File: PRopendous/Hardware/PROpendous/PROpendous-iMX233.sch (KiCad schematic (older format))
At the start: 19 parts, among them IC1 i.MX233, SW1 POWER, X1 24MHz

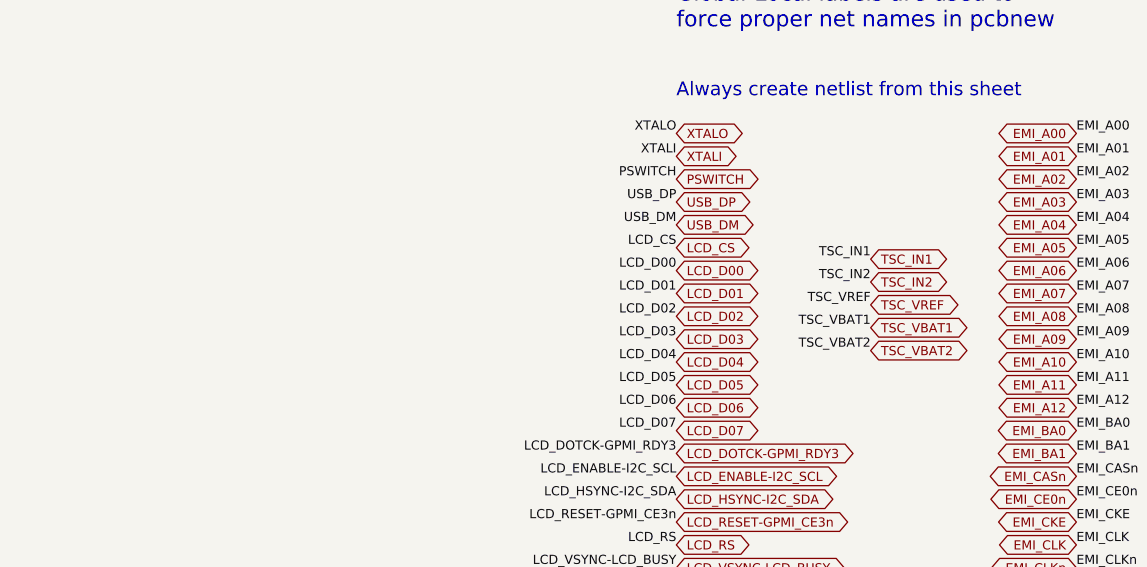
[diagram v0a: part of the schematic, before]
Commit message: Updated i.MX233-based PROpendous board with EEPROM to fix Freescale Errata #2229.
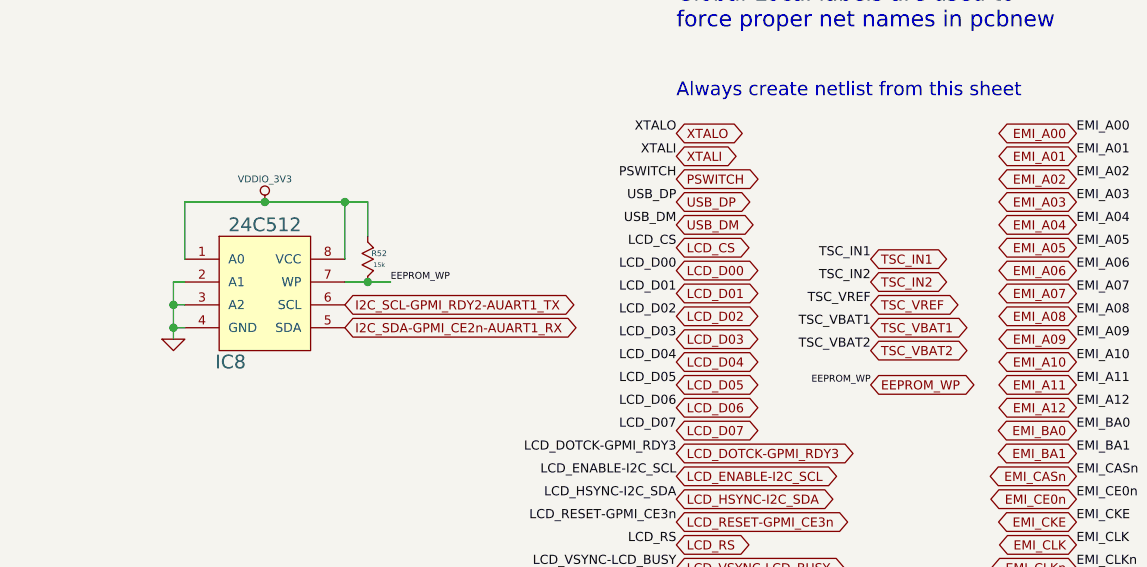
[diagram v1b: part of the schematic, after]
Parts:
- added IC8: 24C512, symbol 24C512
- added R52: 15k, symbol R_MINI
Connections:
- net labels added: EEPROM_WP
- wire segments 52 -> 61
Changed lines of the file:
@@
-EESchema Schematic File Version 2  date 26/04/2010 13:13:01
+EESchema Schematic File Version 2  date 27/04/2010 18:25:33
 LIBS:opendous
 LIBS:device
@@
 Sheet 2 8
 Title "PROpendous"
-Date "26 apr 2010"
+Date "27 apr 2010"
 Rev "1.0"
 Comp "Opendous Inc. (www.opendous.org)"
@@
 Comment4 "www.PROpendous.org"
 $EndDescr
+Text GLabel 9900 2450 2    40   BiDi ~ 0
+EEPROM_WP
+Connection ~ 7700 2000
+Wire Wire Line
+	7800 2000 7600 2000
+Connection ~ 6850 2200
+Wire Wire Line
+	6850 2100 6900 2100
+Connection ~ 7250 1650
+Wire Wire Line
+	6900 1900 6900 1650
 Connection ~ 7450 6050
 Connection ~ 7250 6050
@@
 	7250 6050 7250 5850
 Connection ~ 7450 5950
+Wire Wire Line
+	7600 1650 7600 1900
+Wire Wire Line
+	6850 2200 6900 2200
+Wire Wire Line
+	6900 2000 6850 2000
+Wire Wire Line
+	6850 2000 6850 2250
+Connection ~ 6850 2100
+Wire Wire Line
+	7700 1800 7700 1650
+Wire Wire Line
+	7700 1650 6900 1650
+Connection ~ 7600 1650
+Text Label 9900 2450 2    30   ~ 0
+EEPROM_WP
+Text Label 7800 2000 0    30   ~ 0
+EEPROM_WP
+Text GLabel 7600 2200 2    40   BiDi ~ 0
+I2C_SDA-GPMI_CE2n-AUART1_RX
+Text GLabel 7600 2100 2    40   BiDi ~ 0
+I2C_SCL-GPMI_RDY2-AUART1_TX
+$Comp
+L R_MINI R52
+U 1 1 4BD75B1B
+P 7700 1900
+F 0 "R52" V 7675 1950 25  0000 C CNN
+F 1 "15k" V 7725 1950 20  0000 C CNN
+	1    7700 1900
+	0    1    1    0
+$EndComp
+$Comp
+L GND #PWR01
+U 1 1 4BD75A47
+P 6850 2250
+F 0 "#PWR01" H 6850 2250 30  0001 C CNN
+F 1 "GND" H 6850 2180 30  0001 C CNN
+	1    6850 2250
+	1    0    0    -1
+$EndComp
+$Comp
+L VDDIO_3V3 #PWR02
+U 1 1 4BD75A3A
+P 7250 1650
+F 0 "#PWR02" H 7250 1750 30  0001 C CNN
+F 1 "VDDIO_3V3" H 7250 1750 30  0000 C CNN
+	1    7250 1650
+	1    0    0    -1
+$EndComp
+$Comp
+L 24C512 IC8
+U 1 1 4BD75A33
+P 7250 2050
+F 0 "IC8" H 7100 1750 60  0000 C CNN
+F 1 "24C512" H 7250 2350 60  0000 C CNN
+	1    7250 2050
+	1    0    0    -1
+$EndComp
 $Comp
 L IMX233 IC1
@@
 $EndComp
 $Comp
-L GND #PWR01
+L GND #PWR03
 U 1 1 4BCCECE8
 P 6450 7500
-F 0 "#PWR01" H 6450 7500 30  0001 C CNN
+F 0 "#PWR03" H 6450 7500 30  0001 C CNN
 F 1 "GND" H 6450 7430 30  0001 C CNN
 	1    6450 7500
@@
 $EndComp
 $Comp
-L GND1 #PWR02
+L GND1 #PWR04
 U 1 1 4BCCECDD
 P 6150 7500
-F 0 "#PWR02" H 6150 7500 30  0001 C CNN
+F 0 "#PWR04" H 6150 7500 30  0001 C CNN
 F 1 "GND1" H 6150 7430 30  0000 C CNN
 	1    6150 7500
@@
 Use GNDPWR for chassis\nground ring to suppress EMI
 $Comp
-L GND #PWR03
+L GND #PWR05
 U 1 1 4BCC48BC
 P 7500 6100
-F 0 "#PWR03" H 7500 6100 30  0001 C CNN
+F 0 "#PWR05" H 7500 6100 30  0001 C CNN
 F 1 "GND" H 7500 6030 30  0001 C CNN
 	1    7500 6100
@@
 $EndComp
 $Comp
-L GNDPWR #PWR04
+L GNDPWR #PWR06
 U 1 1 4BCC48B6
 P 7200 6100
-F 0 "#PWR04" H 7200 6150 40  0001 C CNN
+F 0 "#PWR06" H 7200 6150 40  0001 C CNN
 F 1 "GNDPWR" H 7200 6040 25  0000 C CNN
 	1    7200 6100
@@
 $EndComp
 $Comp
-L VDDIO_3V3 #PWR05
+L VDDIO_3V3 #PWR07
 U 1 1 4BC3A9DE
 P 5100 700
-F 0 "#PWR05" H 5100 800 30  0001 C CNN
+F 0 "#PWR07" H 5100 800 30  0001 C CNN
 F 1 "VDDIO_3V3" H 5100 800 30  0000 C CNN
 	1    5100 700
@@
 $EndComp
 $Comp
-L GNDPWR #PWR06
+L GNDPWR #PWR08
 U 1 1 4BBD1ABB
 P 7350 5300
-F 0 "#PWR06" H 7350 5350 40  0001 C CNN
+F 0 "#PWR08" H 7350 5350 40  0001 C CNN
 F 1 "GNDPWR" H 7350 5240 25  0000 C CNN
 	1    7350 5300
@@
 $EndComp
 $Comp
-L HP_VGND #PWR07
+L HP_VGND #PWR09
 U 1 1 4BBCE7B9
 P 4550 7350
-F 0 "#PWR07" H 4550 7350 30  0001 C CNN
+F 0 "#PWR09" H 4550 7350 30  0001 C CNN
 F 1 "HP_VGND" H 4550 7280 30  0000 C CNN
 	1    4550 7350
@@
 PSWITCH
 $Comp
-L GND #PWR08
+L GND #PWR010
 U 1 1 4BBCDC88
 P 1200 2100
-F 0 "#PWR08" H 1200 2100 30  0001 C CNN
+F 0 "#PWR010" H 1200 2100 30  0001 C CNN
 F 1 "GND" H 1200 2030 30  0001 C CNN
 	1    1200 2100
@@
 $EndComp
 $Comp
-L VDD_XTAL #PWR09
+L VDD_XTAL #PWR011
 U 1 1 4BBCDC06
 P 650 1350
-F 0 "#PWR09" H 650 1450 30  0001 C CNN
+F 0 "#PWR011" H 650 1450 30  0001 C CNN
 F 1 "VDD_XTAL" H 650 1450 30  0000 C CNN
 	1    650  1350
@@
 $EndComp
 $Comp
-L GND #PWR010
+L GND #PWR012
 U 1 1 4BBCDB43
 P 650 2100
-F 0 "#PWR010" H 650 2100 30  0001 C CNN
+F 0 "#PWR012" H 650 2100 30  0001 C CNN
 F 1 "GND" H 650 2030 30  0001 C CNN
 	1    650  2100
@@
 $EndComp
 $Comp
-L VDD_XTAL #PWR011
+L VDD_XTAL #PWR013
 U 1 1 4BBCDB1B
 P 650 1800
-F 0 "#PWR011" H 650 1900 30  0001 C CNN
+F 0 "#PWR013" H 650 1900 30  0001 C CNN
 F 1 "VDD_XTAL" H 650 1900 30  0000 C CNN
 	1    650  1800
@@
 $EndComp
 $Comp
-L VDD5V #PWR012
+L VDD5V #PWR014
 U 1 1 4BBCD826
 P 4300 700
-F 0 "#PWR012" H 4300 800 30  0001 C CNN
+F 0 "#PWR014" H 4300 800 30  0001 C CNN
 F 1 "VDD5V" H 4300 800 30  0000 C CNN
 	1    4300 700
@@
 $EndComp
 $Comp
-L GND #PWR013
+L GND #PWR015
 U 1 1 4BBCD031
 P 3950 7350
-F 0 "#PWR013" H 3950 7350 30  0001 C CNN
+F 0 "#PWR015" H 3950 7350 30  0001 C CNN
 F 1 "GND" H 3950 7280 30  0001 C CNN
 	1    3950 7350
@@
 $EndComp
 $Comp
-L GND #PWR014
+L GND #PWR016
 U 1 1 4BBCCF65
 P 1600 600
-F 0 "#PWR014" H 1600 600 30  0001 C CNN
+F 0 "#PWR016" H 1600 600 30  0001 C CNN
 F 1 "GND" H 1600 530 30  0001 C CNN
 	1    1600 600
@@
 GND1 must route to\nstar ground at VSSA2
 $Comp
-L GND1 #PWR015
+L GND1 #PWR017
 U 1 1 4BBCCEB7
 P 5850 7100
-F 0 "#PWR015" H 5850 7100 30  0001 C CNN
+F 0 "#PWR017" H 5850 7100 30  0001 C CNN
 F 1 "GND1" H 5850 7030 30  0000 C CNN
 	1    5850 7100
@@
 $EndComp
 $Comp
-L VDDM_2V5 #PWR016
+L VDDM_2V5 #PWR018
 U 1 1 4BBCCC9E
 P 4750 700
-F 0 "#PWR016" H 4750 800 30  0001 C CNN
+F 0 "#PWR018" H 4750 800 30  0001 C CNN
 F 1 "VDDM_2V5" H 4750 800 30  0000 C CNN
 	1    4750 700
@@
 $EndComp
 $Comp
-L VDD_XTAL #PWR017
+L VDD_XTAL #PWR019
 U 1 1 4BBCCC78
 P 4450 850
-F 0 "#PWR017" H 4450 950 30  0001 C CNN
+F 0 "#PWR019" H 4450 950 30  0001 C CNN
 F 1 "VDD_XTAL" H 4450 950 30  0000 C CNN
 	1    4450 850
@@
 $EndComp
 $Comp
-L VDDA #PWR018
+L VDDA #PWR020
 U 1 1 4BBCCB4A
 P 4100 700
-F 0 "#PWR018" H 4100 800 30  0001 C CNN
+F 0 "#PWR020" H 4100 800 30  0001 C CNN
 F 1 "VDDA" H 4100 800 30  0000 C CNN
 	1    4100 700
@@
 $EndComp
 $Comp
-L VDDD #PWR019
+L VDDD #PWR021
 U 1 1 4BBCCB16
 P 3800 700
-F 0 "#PWR019" H 3800 800 30  0001 C CNN
+F 0 "#PWR021" H 3800 800 30  0001 C CNN
 F 1 "VDDD" H 3800 800 30  0000 C CNN
 	1    3800 700
@@
 $EndComp
 $Comp
-L VDDIO_3V3 #PWR020
+L VDDIO_3V3 #PWR022
 U 1 1 4BBCC974
 P 3550 700
-F 0 "#PWR020" H 3550 800 30  0001 C CNN
+F 0 "#PWR022" H 3550 800 30  0001 C CNN
 F 1 "VDDIO_3V3" H 3550 800 30  0000 C CNN
 	1    3550 700
@@
 $EndComp
 $Comp
-L VDD4P2 #PWR021
+L VDD4P2 #PWR023
 U 1 1 4BBCC950
 P 3050 700
-F 0 "#PWR021" H 3050 800 30  0001 C CNN
+F 0 "#PWR023" H 3050 800 30  0001 C CNN
 F 1 "VDD4P2" H 3050 800 30  0000 C CNN
 	1    3050 700
@@
 $EndComp
 $Comp
-L VDD_BATT #PWR022
+L VDD_BATT #PWR024
 U 1 1 4BBCC942
 P 2800 700
-F 0 "#PWR022" H 2800 800 30  0001 C CNN
+F 0 "#PWR024" H 2800 800 30  0001 C CNN
 F 1 "VDD_BATT" H 2800 800 30  0000 C CNN
 	1    2800 700

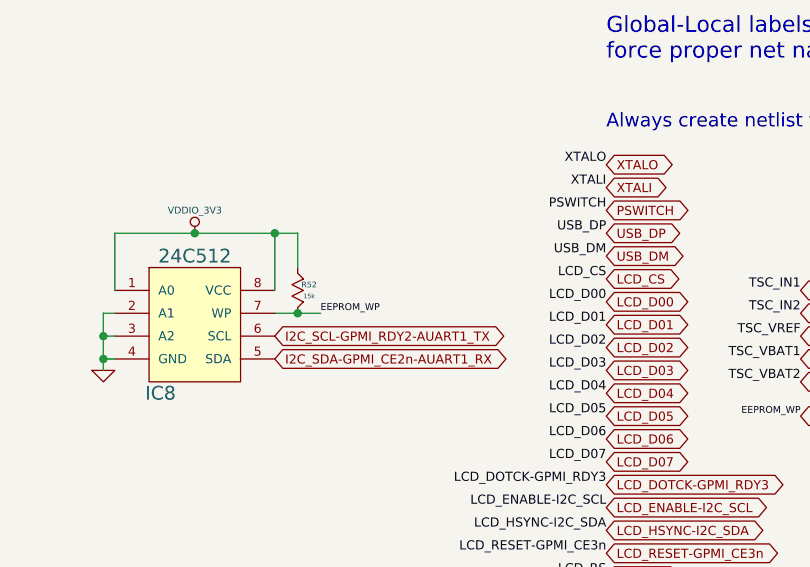
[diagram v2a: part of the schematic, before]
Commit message: Updated PROpendous design and manufacturing files.
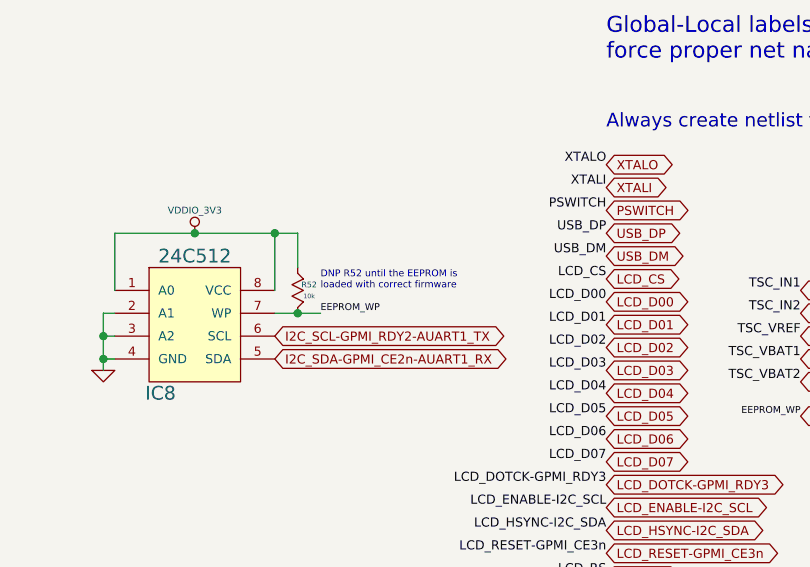
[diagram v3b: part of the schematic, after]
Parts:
- R52: value 15k -> 10k
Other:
- note added: "DNP R52 until the EEPROM is\nloaded with correct firmware"
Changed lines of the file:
@@
-EESchema Schematic File Version 2  date 07/05/2010 11:28:22
+EESchema Schematic File Version 2  date 18/05/2010 10:44:52
 LIBS:opendous
 LIBS:device
@@
 LIBS:valves
 LIBS:power
+LIBS:PROpendous-cache
 EELAYER 24  0
 EELAYER END
@@
 Sheet 2 8
 Title "PROpendous"
-Date "7 may 2010"
+Date "18 may 2010"
 Rev "1.0"
 Comp "Opendous Inc. (www.opendous.org)"
@@
 Comment4 "www.PROpendous.org"
 $EndDescr
+Text Notes 7800 1900 0    30   ~ 0
+DNP R52 until the EEPROM is\nloaded with correct firmware
 Text GLabel 9900 2450 2    40   BiDi ~ 0
 EEPROM_WP
@@
 P 7700 1900
 F 0 "R52" V 7675 1950 25  0000 C CNN
-F 1 "15k" V 7725 1950 20  0000 C CNN
+F 1 "10k" V 7725 1950 20  0000 C CNN
 	1    7700 1900
 	0    1    1    0

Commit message: Updated PROpendous with correct I2C EEPROM address.  Added pictures of the LPC3130 based PROpendous-DIY.
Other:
- note added: "I2C EEPROM Address = 0b1010000R = 0xA0 = 160"
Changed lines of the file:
@@
-EESchema Schematic File Version 2  date 31/05/2010 00:35:42
+EESchema Schematic File Version 2  date 07/06/2010 07:15:05
 LIBS:opendous
 LIBS:device
@@
 LIBS:valves
 LIBS:power
+LIBS:PROpendous-cache
 EELAYER 24  0
 EELAYER END
@@
 Sheet 2 8
 Title "PROpendous"
-Date "29 may 2010"
+Date "7 jun 2010"
 Rev "1.0"
 Comp "Opendous Inc. (www.opendous.org)"
@@
 Comment4 "www.PROpendous.org"
 $EndDescr
+Text Notes 6800 2500 0    40   ~ 0
+I2C EEPROM Address = 0b1010000R = 0xA0 = 160
+Connection ~ 6850 2000
+Wire Wire Line
+	6850 2250 6850 1900
+Wire Wire Line
+	6850 1900 6900 1900
+Connection ~ 7600 1650
+Wire Wire Line
+	7250 1650 7700 1650
+Wire Wire Line
+	7700 1650 7700 1800
+Connection ~ 6850 2100
+Wire Wire Line
+	6850 2000 6900 2000
+Wire Wire Line
+	6850 2200 6900 2200
+Wire Wire Line
+	7600 1650 7600 1900
+Connection ~ 7450 5950
+Wire Wire Line
+	7250 5850 7250 6050
+Wire Wire Line
+	7500 6100 7500 6050
+Wire Wire Line
+	7500 6050 7450 6050
+Connection ~ 4750 950
+Wire Wire Line
+	4750 950  4750 700
+Connection ~ 4800 950
+Wire Wire Line
+	5050 950  5150 950
+Wire Wire Line
+	7350 5300 7350 5250
+Connection ~ 3950 7250
+Wire Wire Line
+	3950 7250 3950 7350
+Connection ~ 4000 7250
+Connection ~ 3800 7250
+Wire Wire Line
+	1100 1250 1100 1200
+Wire Wire Line
+	1100 1550 1100 1450
+Wire Wire Line
+	1050 1500 1350 1500
+Wire Wire Line
+	1550 1500 2200 1500
+Wire Wire Line
+	1100 1850 1100 1750
+Wire Wire Line
+	1200 2100 1200 2050
+Wire Wire Line
+	650  2100 650  2050
+Wire Wire Line
+	5850 6800 5850 6700
+Wire Wire Line
+	5850 6700 5700 6700
+Connection ~ 1300 900
+Wire Wire Line
+	2200 1300 1300 1300
+Wire Wire Line
+	1300 1300 1300 750
+Connection ~ 1600 550
+Wire Wire Line
+	1600 600  1600 550
+Wire Wire Line
+	4450 850  4450 950
+Wire Wire Line
+	3550 950  3550 700
+Wire Wire Line
+	3800 700  3800 950
+Wire Wire Line
+	4150 950  4050 950
+Wire Wire Line
+	3200 900  3200 950
+Connection ~ 2800 950
+Wire Wire Line
+	2900 950  2800 950
+Wire Wire Line
+	2800 950  2800 700
+Wire Wire Line
+	3050 950  3050 700
+Wire Wire Line
+	3400 900  3400 950
+Wire Wire Line
+	4100 700  4100 950
+Connection ~ 4100 950
+Wire Wire Line
+	3900 950  3700 950
+Connection ~ 3800 950
+Wire Wire Line
+	4300 700  4300 950
+Wire Wire Line
+	1900 550  1300 550
+Wire Wire Line
+	1900 750  1900 1200
+Wire Wire Line
+	1900 1200 2200 1200
+Connection ~ 1900 900
+Wire Wire Line
+	5850 7000 5850 7100
+Wire Wire Line
+	650  1850 650  1800
+Wire Wire Line
+	750  1500 650  1500
+Wire Wire Line
+	1300 1900 1300 2050
+Wire Wire Line
+	1300 2050 1100 2050
+Connection ~ 1200 2050
+Wire Wire Line
+	650  1500 650  1350
+Connection ~ 1100 1500
+Wire Wire Line
+	1300 1700 1300 1500
+Connection ~ 1300 1500
+Connection ~ 3900 7250
+Wire Wire Line
+	4250 7250 3650 7250
+Connection ~ 4150 7250
+Wire Wire Line
+	4550 7350 4550 7250
+Wire Wire Line
+	4600 950  4900 950
+Connection ~ 4700 950
+Wire Wire Line
+	5100 700  5100 950
+Connection ~ 5100 950
+Wire Wire Line
+	7250 6050 7200 6050
+Wire Wire Line
+	7200 6050 7200 6100
+Wire Wire Line
+	6150 7500 6150 7450
+Wire Wire Line
+	6150 7450 6200 7450
+Wire Wire Line
+	6400 7450 6450 7450
+Wire Wire Line
+	6450 7450 6450 7500
+Connection ~ 7250 5950
+Wire Wire Line
+	7450 6050 7450 5850
+Connection ~ 7250 6050
+Connection ~ 7450 6050
+Wire Wire Line
+	6850 2100 6900 2100
+Connection ~ 6850 2200
+Wire Wire Line
+	7600 2000 7800 2000
+Connection ~ 7700 2000
 Text Notes 7800 1900 0    30   ~ 0
 DNP R52 until the EEPROM is\nloaded with correct firmware
 Text GLabel 9900 2450 2    40   BiDi ~ 0
 EEPROM_WP
-Connection ~ 7700 2000
-Wire Wire Line
-	7800 2000 7600 2000
-Connection ~ 6850 2200
-Wire Wire Line
-	6850 2100 6900 2100
-Connection ~ 7250 1650
-Wire Wire Line
-	6900 1900 6900 1650
-Connection ~ 7450 6050
-Connection ~ 7250 6050
-Wire Wire Line
-	7450 5850 7450 6050
-Connection ~ 7250 5950
-Wire Wire Line
-	6450 7500 6450 7450
-Wire Wire Line
-	6450 7450 6400 7450
-Wire Wire Line
-	6200 7450 6150 7450
-Wire Wire Line
-	6150 7450 6150 7500
-Wire Wire Line
-	7200 6100 7200 6050
-Wire Wire Line
-	7200 6050 7250 6050
-Connection ~ 5100 950
-Wire Wire Line
-	5100 700  5100 950
-Connection ~ 4700 950
-Wire Wire Line
-	4900 950  4600 950
-Wire Wire Line
-	4550 7350 4550 7250
-Connection ~ 4150 7250
-Wire Wire Line
-	3650 7250 4250 7250
-Connection ~ 3900 7250
-Connection ~ 1300 1500
-Wire Wire Line
-	1300 1700 1300 1500
-Connection ~ 1100 1500
-Wire Wire Line
-	650  1350 650  1500
-Connection ~ 1200 2050
-Wire Wire Line
-	1100 2050 1300 2050
-Wire Wire Line
-	1300 2050 1300 1900
-Wire Wire Line
-	650  1500 750  1500
-Wire Wire Line
-	650  1850 650  1800
-Wire Wire Line
-	5850 7000 5850 7100
-Connection ~ 1900 900
-Wire Wire Line
-	2200 1200 1900 1200
-Wire Wire Line
-	1900 1200 1900 750
-Wire Wire Line
-	1300 550  1900 550
-Wire Wire Line
-	4300 700  4300 950
-Connection ~ 3800 950
-Wire Wire Line
-	3700 950  3900 950
-Connection ~ 4100 950
-Wire Wire Line
-	4100 700  4100 950
-Wire Wire Line
-	3400 900  3400 950
-Wire Wire Line
-	3050 950  3050 700
-Wire Wire Line
-	2800 700  2800 950
-Wire Wire Line
-	2800 950  2900 950
-Connection ~ 2800 950
-Wire Wire Line
-	3200 900  3200 950
-Wire Wire Line
-	4050 950  4150 950
-Wire Wire Line
-	3800 700  3800 950
-Wire Wire Line
-	3550 950  3550 700
-Wire Wire Line
-	4450 850  4450 950
-Wire Wire Line
-	1600 600  1600 550
-Connection ~ 1600 550
-Wire Wire Line
-	1300 750  1300 1300
-Wire Wire Line
-	1300 1300 2200 1300
-Connection ~ 1300 900
-Wire Wire Line
-	5700 6700 5850 6700
-Wire Wire Line
-	5850 6700 5850 6800
-Wire Wire Line
-	650  2100 650  2050
-Wire Wire Line
-	1200 2100 1200 2050
-Wire Wire Line
-	1100 1850 1100 1750
-Wire Wire Line
-	1550 1500 2200 1500
-Wire Wire Line
-	1350 1500 1050 1500
-Wire Wire Line
-	1100 1450 1100 1550
-Wire Wire Line
-	1100 1250 1100 1200
-Connection ~ 3800 7250
-Connection ~ 4000 7250
-Wire Wire Line
-	3950 7250 3950 7350
-Connection ~ 3950 7250
-Wire Wire Line
-	7350 5300 7350 5250
-Wire Wire Line
-	5150 950  5050 950
-Connection ~ 4800 950
-Wire Wire Line
-	4750 950  4750 700
-Connection ~ 4750 950
-Wire Wire Line
-	7450 6050 7500 6050
-Wire Wire Line
-	7500 6050 7500 6100
-Wire Wire Line
-	7250 6050 7250 5850
-Connection ~ 7450 5950
-Wire Wire Line
-	7600 1650 7600 1900
-Wire Wire Line
-	6850 2200 6900 2200
-Wire Wire Line
-	6900 2000 6850 2000
-Wire Wire Line
-	6850 2000 6850 2250
-Connection ~ 6850 2100
-Wire Wire Line
-	7700 1800 7700 1650
-Wire Wire Line
-	7700 1650 6900 1650
-Connection ~ 7600 1650
 Text Label 9900 2450 2    30   ~ 0
 EEPROM_WP

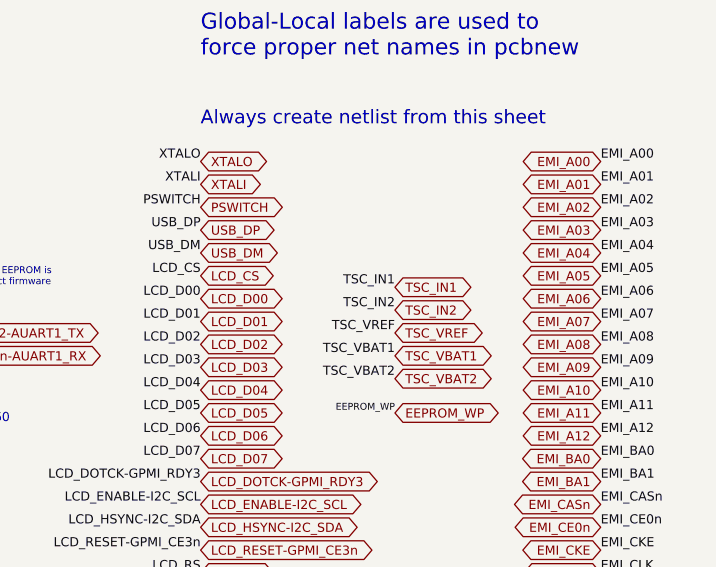
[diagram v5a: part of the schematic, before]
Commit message: Switch to ceramic capacitors for bulk decoupling which are less expensive than similarly low-ESR tantalum capacitors.
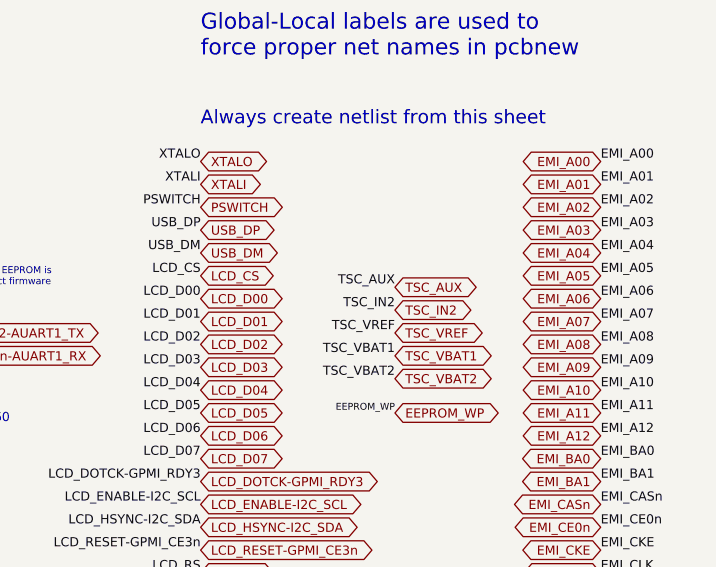
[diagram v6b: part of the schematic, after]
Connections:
- net labels added: TSC_AUX
- net labels removed: TSC_IN1
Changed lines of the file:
@@
-EESchema Schematic File Version 2  date 07/06/2010 07:15:05
+EESchema Schematic File Version 2  date 17/06/2010 09:45:34
 LIBS:opendous
 LIBS:device
@@
 LIBS:valves
 LIBS:power
-LIBS:PROpendous-cache
 EELAYER 24  0
 EELAYER END
@@
 Sheet 2 8
 Title "PROpendous"
-Date "7 jun 2010"
+Date "17 jun 2010"
 Rev "1.0"
 Comp "Opendous Inc. (www.opendous.org)"
@@
 TSC_IN2
 Text Label 9900 1900 2    40   ~ 0
-TSC_IN1
+TSC_AUX
 Text Notes 6800 6300 0    50   ~ 0
 Use GNDPWR for chassis\nground ring to suppress EMI
@@
 PSWITCH
 Text GLabel 9900 1900 2    40   BiDi ~ 0
-TSC_IN1
+TSC_AUX
 Text GLabel 9900 2000 2    40   BiDi ~ 0
 TSC_IN2
